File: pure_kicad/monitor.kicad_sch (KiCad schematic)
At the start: 46 parts, among them J3 XT60M, J4 XT60M, J5 Conn_01x04_Pin, J6 Conn_01x04_Pin, Q5 Q_PMOS_SGD, Q6 Q_NMOS_DGS, Q8 Q_NMOS_DGS, U2 BQ40Z80RSMR

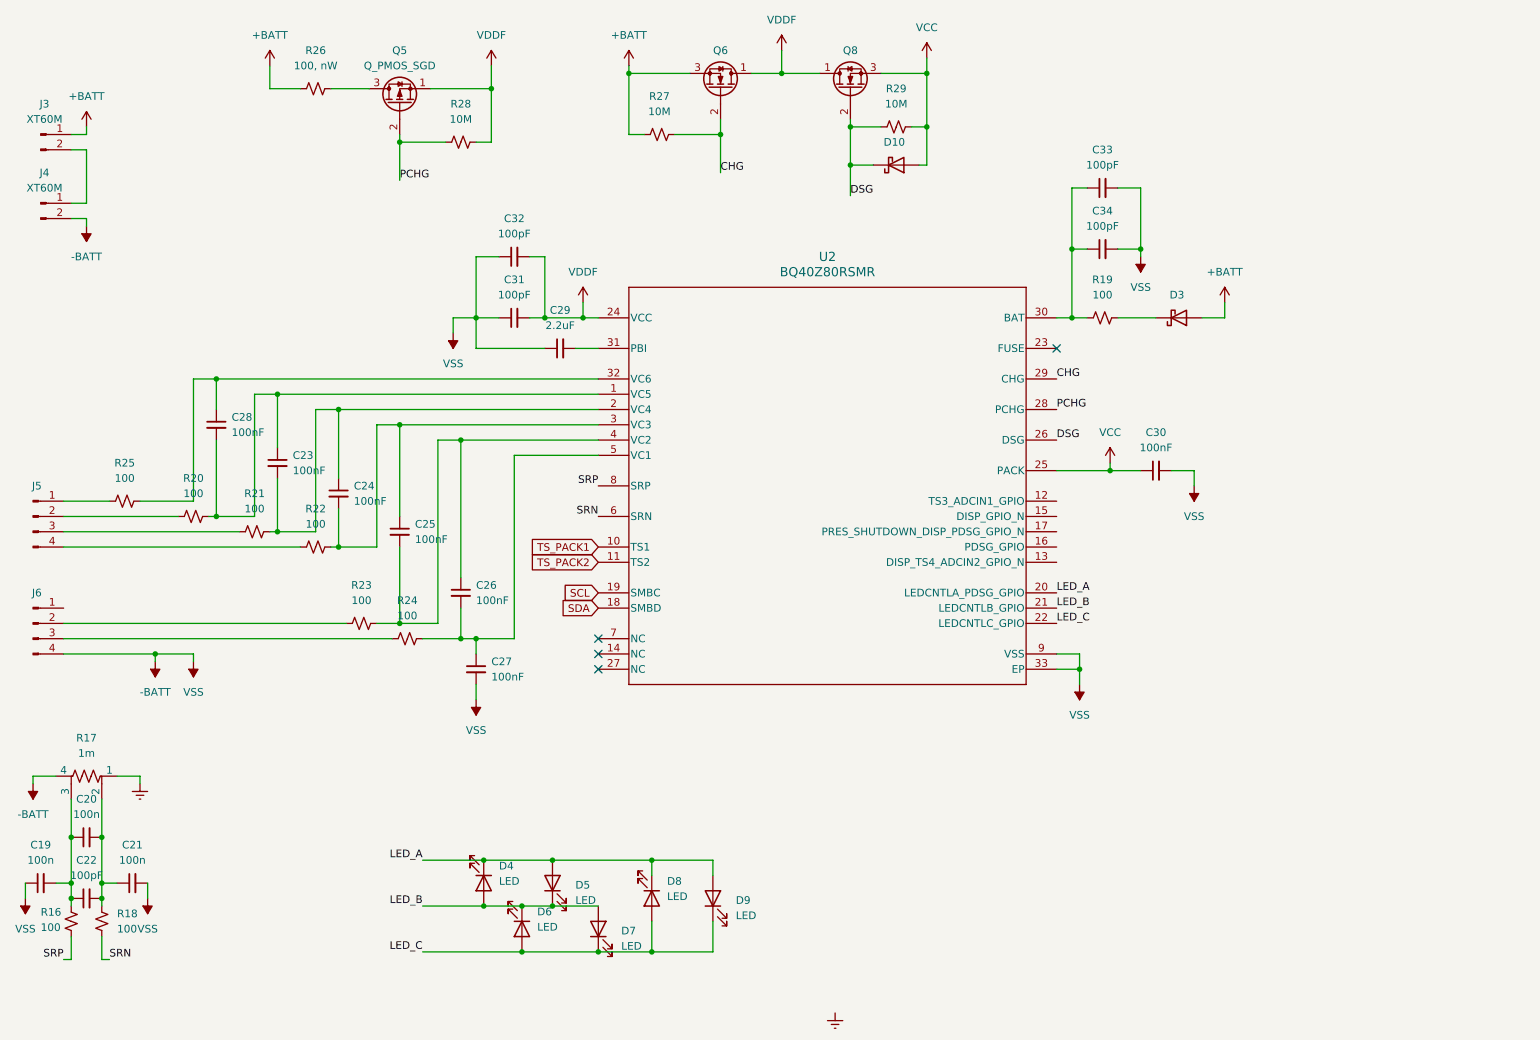
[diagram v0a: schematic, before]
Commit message: Assign parts, start layout
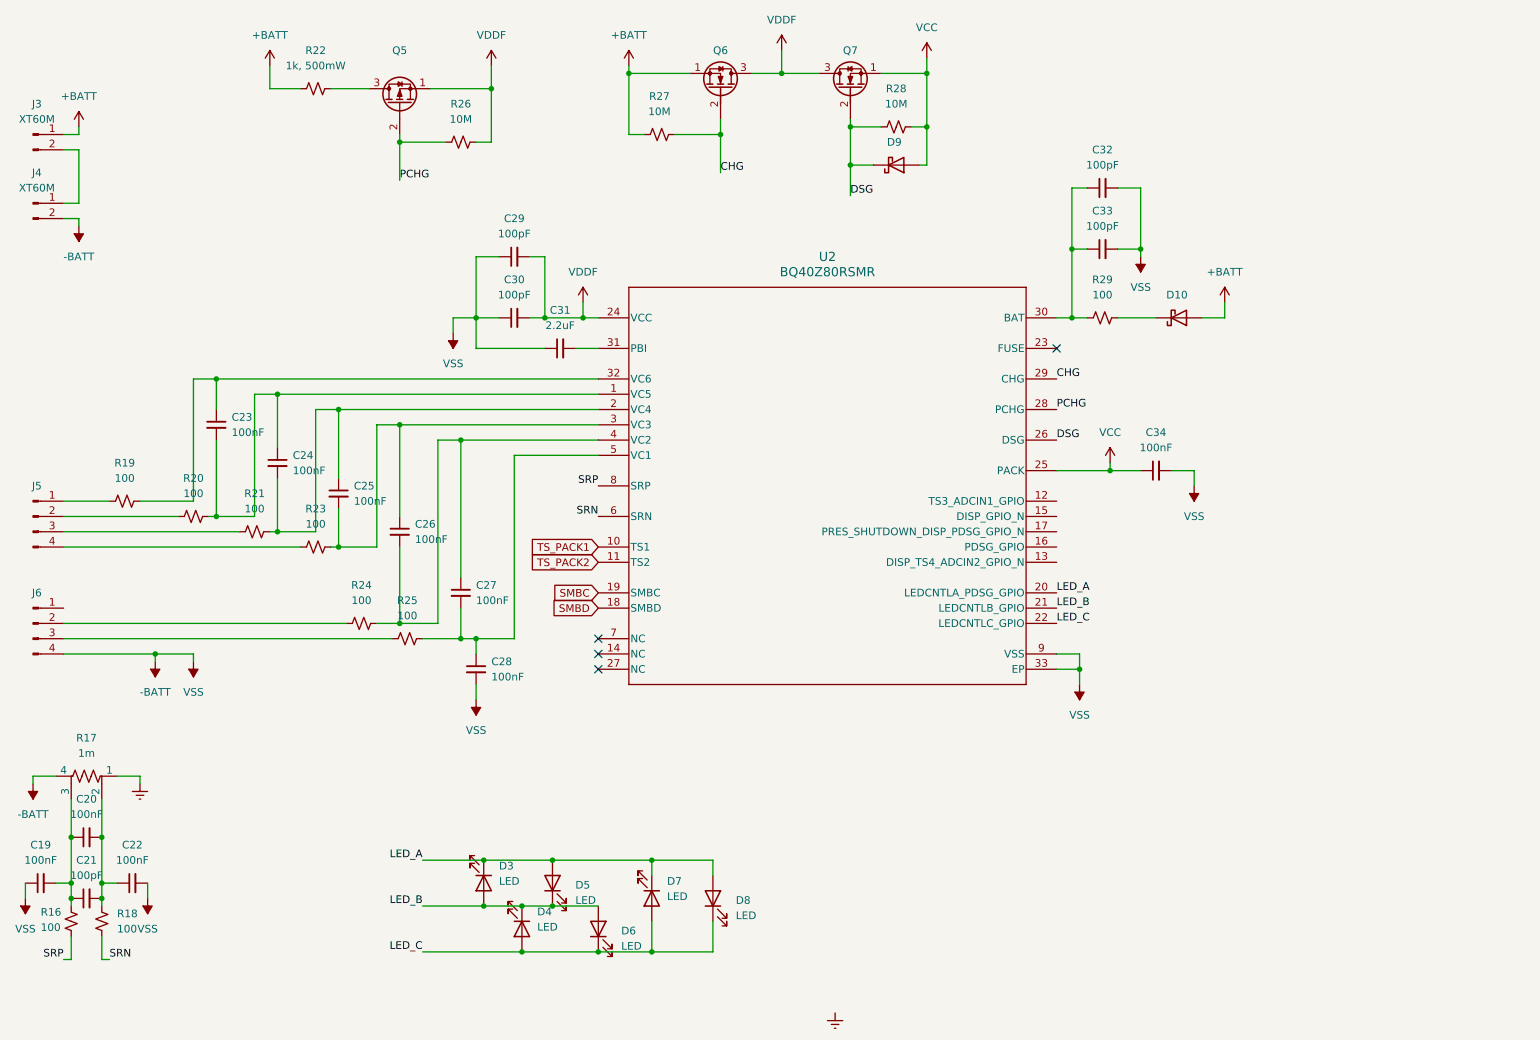
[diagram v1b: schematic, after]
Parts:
- C19, C20: value 100n -> 100nF; footprint Capacitor_SMD:C_0402_1005Metric_Pad0.74x0.62mm_HandSolder -> Capacitor_SMD:C_0603_1608Metric_Pad1.08x0.95mm_HandSolder
- C21: renamed from C22; footprint Capacitor_SMD:C_0402_1005Metric_Pad0.74x0.62mm_HandSolder -> Capacitor_SMD:C_0603_1608Metric_Pad1.08x0.95mm_HandSolder
- C22: renamed from C21; value 100n -> 100nF; footprint Capacitor_SMD:C_0402_1005Metric_Pad0.74x0.62mm_HandSolder -> Capacitor_SMD:C_0603_1608Metric_Pad1.08x0.95mm_HandSolder
- C23: renamed from C28; footprint (none) -> Capacitor_SMD:C_0603_1608Metric_Pad1.08x0.95mm_HandSolder
- C24: renamed from C23; footprint (none) -> Capacitor_SMD:C_0603_1608Metric_Pad1.08x0.95mm_HandSolder
- C25: renamed from C24; footprint (none) -> Capacitor_SMD:C_0603_1608Metric_Pad1.08x0.95mm_HandSolder
- C26: renamed from C25; footprint (none) -> Capacitor_SMD:C_0603_1608Metric_Pad1.08x0.95mm_HandSolder
- C27: renamed from C26; footprint (none) -> Capacitor_SMD:C_0603_1608Metric_Pad1.08x0.95mm_HandSolder
- C28: renamed from C27; footprint (none) -> Capacitor_SMD:C_0603_1608Metric_Pad1.08x0.95mm_HandSolder
- C29: renamed from C32; footprint Capacitor_SMD:C_0402_1005Metric_Pad0.74x0.62mm_HandSolder -> Capacitor_SMD:C_0603_1608Metric_Pad1.08x0.95mm_HandSolder
- C30: renamed from C31; footprint Capacitor_SMD:C_0402_1005Metric_Pad0.74x0.62mm_HandSolder -> Capacitor_SMD:C_0603_1608Metric_Pad1.08x0.95mm_HandSolder
- C31: renamed from C29; footprint Capacitor_SMD:C_0402_1005Metric_Pad0.74x0.62mm_HandSolder -> Capacitor_SMD:C_0603_1608Metric_Pad1.08x0.95mm_HandSolder
- C32: renamed from C33; footprint Capacitor_SMD:C_0402_1005Metric_Pad0.74x0.62mm_HandSolder -> Capacitor_SMD:C_0603_1608Metric_Pad1.08x0.95mm_HandSolder
- C33: renamed from C34; footprint Capacitor_SMD:C_0402_1005Metric_Pad0.74x0.62mm_HandSolder -> Capacitor_SMD:C_0603_1608Metric_Pad1.08x0.95mm_HandSolder
- C34: renamed from C30; footprint (none) -> Capacitor_SMD:C_0603_1608Metric_Pad1.08x0.95mm_HandSolder
- D10: renamed from D3; footprint (none) -> Diode_SMD:D_SMA_Handsoldering
- D9: renamed from D10; footprint (none) -> Diode_SMD:D_SMA_Handsoldering
- Q5: footprint (none) -> cyberec:DFN-8_L3.0-W3.0-P0.65-BL-4
- Q6: footprint (none) -> cyberec:DFN-8_L3.0-W3.0-P0.65-BL-4; symbol Transistor_FET:Q_NMOS_DGS -> Transistor_FET:Q_NMOS_SGD
- Q7: renamed from Q8; footprint (none) -> cyberec:DFN-8_L3.0-W3.0-P0.65-BL-4; symbol Transistor_FET:Q_NMOS_DGS -> Transistor_FET:Q_NMOS_SGD
- R17: footprint (none) -> cyberec:R1206-sense-handsolder
- R18, R20, R21: footprint Resistor_SMD:R_0402_1005Metric_Pad0.72x0.64mm_HandSolder -> Resistor_SMD:R_0603_1608Metric_Pad0.98x0.95mm_HandSolder
- R19: renamed from R25; footprint Resistor_SMD:R_0402_1005Metric_Pad0.72x0.64mm_HandSolder -> Resistor_SMD:R_0603_1608Metric_Pad0.98x0.95mm_HandSolder
- R22: renamed from R26; value 100, nW -> 1k, 500mW; footprint Resistor_SMD:R_0402_1005Metric_Pad0.72x0.64mm_HandSolder -> Resistor_SMD:R_1210_3225Metric_Pad1.30x2.65mm_HandSolder
- R23: renamed from R22; footprint Resistor_SMD:R_0402_1005Metric_Pad0.72x0.64mm_HandSolder -> Resistor_SMD:R_0603_1608Metric_Pad0.98x0.95mm_HandSolder
- R24: renamed from R23; footprint Resistor_SMD:R_0402_1005Metric_Pad0.72x0.64mm_HandSolder -> Resistor_SMD:R_0603_1608Metric_Pad0.98x0.95mm_HandSolder
- R25: renamed from R24; footprint Resistor_SMD:R_0402_1005Metric_Pad0.72x0.64mm_HandSolder -> Resistor_SMD:R_0603_1608Metric_Pad0.98x0.95mm_HandSolder
- R29: renamed from R19; footprint Resistor_SMD:R_0402_1005Metric_Pad0.72x0.64mm_HandSolder -> Resistor_SMD:R_0603_1608Metric_Pad0.98x0.95mm_HandSolder
- renumbered D4 to D3, D6 to D4, D7 to D6, D8 to D7, D9 to D8, R28 to R26, R29 to R28
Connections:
- net +BATT: now also Q6.1 (S); no longer Q6.3 (S)
- net VCC: now also Q7.1 (S); no longer Q7.3 (S)
- net VDDF: now also Q6.3 (D), Q7.3 (D); no longer Q6.1 (D), Q7.1 (D)
- net SCL renamed SMBC
- net SDA renamed SMBD
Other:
- moved on the sheet: J3, J4

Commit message: Layout starting to look alright
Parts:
- R16: footprint Resistor_SMD:R_0402_1005Metric_Pad0.72x0.64mm_HandSolder -> Resistor_SMD:R_0603_1608Metric_Pad0.98x0.95mm_HandSolder
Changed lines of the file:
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@@
 			)
 		)
-		(property "Footprint" "Resistor_SMD:R_0402_1005Metric_Pad0.72x0.64mm_HandSolder"
+		(property "Footprint" "Resistor_SMD:R_0603_1608Metric_Pad0.98x0.95mm_HandSolder"
 			(at 36.83 173.99 0)
 			(effects

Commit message: Import all the footprints, use project local 3d files
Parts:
- C19, C20, C21, C22, C23, C24, C25, C26, C27, C28, C29, C30, C31, C32, C33, C34: footprint Capacitor_SMD:C_0603_1608Metric_Pad1.08x0.95mm_HandSolder -> cyberec:C_0603_1608Metric_Pad1.08x0.95mm_HandSolder
- D10, D9: footprint Diode_SMD:D_SMA_Handsoldering -> cyberec:D_SMA_Handsoldering
- D3, D4, D5, D6, D7, D8: footprint LED_SMD:LED_0603_1608Metric_Pad1.05x0.95mm_HandSolder -> cyberec:LED_0603_1608Metric_Pad1.05x0.95mm_HandSolder
- J3, J4: footprint Connector_AMASS:AMASS_XT60-M_1x02_P7.20mm_Vertical -> cyberec:AMASS_XT60-M_1x02_P7.20mm_Vertical
- J5, J6: footprint Connector_JST:JST_XH_B4B-XH-A_1x04_P2.50mm_Vertical -> cyberec:JST_XH_B4B-XH-A_1x04_P2.50mm_Vertical
- R16, R18, R19, R20, R21, R23, R24, R25, R29: footprint Resistor_SMD:R_0603_1608Metric_Pad0.98x0.95mm_HandSolder -> cyberec:R_0603_1608Metric_Pad0.98x0.95mm_HandSolder
- R22: footprint Resistor_SMD:R_1210_3225Metric_Pad1.30x2.65mm_HandSolder -> cyberec:R_1210_3225Metric_Pad1.30x2.65mm_HandSolder
- R26, R27, R28: footprint Resistor_SMD:R_0402_1005Metric_Pad0.72x0.64mm_HandSolder -> cyberec:R_0402_1005Metric_Pad0.72x0.64mm_HandSolder
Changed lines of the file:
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@@
 			)
 		)
-		(property "Footprint" "LED_SMD:LED_0603_1608Metric_Pad1.05x0.95mm_HandSolder"
+		(property "Footprint" "cyberec:LED_0603_1608Metric_Pad1.05x0.95mm_HandSolder"
 			(at 105.41 167.64 0)
 			(effects
@@
 			)
 		)
-		(property "Footprint" "Resistor_SMD:R_0603_1608Metric_Pad0.98x0.95mm_HandSolder"
+		(property "Footprint" "cyberec:R_0603_1608Metric_Pad0.98x0.95mm_HandSolder"
 			(at 77.47 111.76 0)
 			(effects
@@
 			)
 		)
-		(property "Footprint" "Connector_JST:JST_XH_B4B-XH-A_1x04_P2.50mm_Vertical"
+		(property "Footprint" "cyberec:JST_XH_B4B-XH-A_1x04_P2.50mm_Vertical"
 			(at 30.48 106.68 0)
 			(effects
@@
 			)
 		)
-		(property "Footprint" "Resistor_SMD:R_0603_1608Metric_Pad0.98x0.95mm_HandSolder"
+		(property "Footprint" "cyberec:R_0603_1608Metric_Pad0.98x0.95mm_HandSolder"
 			(at 45.72 104.14 0)
 			(effects
@@
 			)
 		)
-		(property "Footprint" "Capacitor_SMD:C_0603_1608Metric_Pad1.08x0.95mm_HandSolder"
+		(property "Footprint" "cyberec:C_0603_1608Metric_Pad1.08x0.95mm_HandSolder"
 			(at 31.75 167.64 0)
 			(effects
@@
 			)
 		)
-		(property "Footprint" "Capacitor_SMD:C_0603_1608Metric_Pad1.08x0.95mm_HandSolder"
+		(property "Footprint" "cyberec:C_0603_1608Metric_Pad1.08x0.95mm_HandSolder"
 			(at 71.12 97.79 0)
 			(effects
@@
 			)
 		)
-		(property "Footprint" "Capacitor_SMD:C_0603_1608Metric_Pad1.08x0.95mm_HandSolder"
+		(property "Footprint" "cyberec:C_0603_1608Metric_Pad1.08x0.95mm_HandSolder"
 			(at 217.17 99.06 0)
 			(effects
@@
 			)
 		)
-		(property "Footprint" "Resistor_SMD:R_0402_1005Metric_Pad0.72x0.64mm_HandSolder"
+		(property "Footprint" "cyberec:R_0402_1005Metric_Pad0.72x0.64mm_HandSolder"
 			(at 134.62 43.18 0)
 			(effects
@@
 			)
 		)
-		(property "Footprint" "Diode_SMD:D_SMA_Handsoldering"
+		(property "Footprint" "cyberec:D_SMA_Handsoldering"
 			(at 173.99 48.26 0)
 			(effects
@@
 			)
 		)
-		(property "Footprint" "Capacitor_SMD:C_0603_1608Metric_Pad1.08x0.95mm_HandSolder"
+		(property "Footprint" "cyberec:C_0603_1608Metric_Pad1.08x0.95mm_HandSolder"
 			(at 208.28 52.07 0)
 			(effects
@@
 			)
 		)
-		(property "Footprint" "Diode_SMD:D_SMA_Handsoldering"
+		(property "Footprint" "cyberec:D_SMA_Handsoldering"
 			(at 220.98 73.66 0)
 			(effects
@@
 			)
 		)
-		(property "Footprint" "Resistor_SMD:R_1210_3225Metric_Pad1.30x2.65mm_HandSolder"
+		(property "Footprint" "cyberec:R_1210_3225Metric_Pad1.30x2.65mm_HandSolder"
 			(at 77.47 35.56 0)
 			(effects
@@
 			)
 		)
-		(property "Footprint" "Capacitor_SMD:C_0603_1608Metric_Pad1.08x0.95mm_HandSolder"
+		(property "Footprint" "cyberec:C_0603_1608Metric_Pad1.08x0.95mm_HandSolder"
 			(at 110.49 63.5 0)
 			(effects
@@
 			)
 		)
-		(property "Footprint" "Resistor_SMD:R_0603_1608Metric_Pad0.98x0.95mm_HandSolder"
+		(property "Footprint" "cyberec:R_0603_1608Metric_Pad0.98x0.95mm_HandSolder"
 			(at 85.09 124.46 0)
 			(effects
@@
 			)
 		)
-		(property "Footprint" "Resistor_SMD:R_0603_1608Metric_Pad0.98x0.95mm_HandSolder"
+		(property "Footprint" "cyberec:R_0603_1608Metric_Pad0.98x0.95mm_HandSolder"
 			(at 92.71 127 0)
 			(effects
@@
 			)
 		)
-		(property "Footprint" "Resistor_SMD:R_0603_1608Metric_Pad0.98x0.95mm_HandSolder"
+		(property "Footprint" "cyberec:R_0603_1608Metric_Pad0.98x0.95mm_HandSolder"
 			(at 36.83 173.99 0)
 			(effects
@@
 			)
 		)
-		(property "Footprint" "Connector_AMASS:AMASS_XT60-M_1x02_P7.20mm_Vertical"
+		(property "Footprint" "cyberec:AMASS_XT60-M_1x02_P7.20mm_Vertical"
 			(at 30.48 43.18 0)
 			(effects
@@
 			)
 		)
-		(property "Footprint" "LED_SMD:LED_0603_1608Metric_Pad1.05x0.95mm_HandSolder"
+		(property "Footprint" "cyberec:LED_0603_1608Metric_Pad1.05x0.95mm_HandSolder"
 			(at 133.35 170.18 0)
 			(effects
@@
 			)
 		)
-		(property "Footprint" "LED_SMD:LED_0603_1608Metric_Pad1.05x0.95mm_HandSolder"
+		(property "Footprint" "cyberec:LED_0603_1608Metric_Pad1.05x0.95mm_HandSolder"
 			(at 124.46 175.26 0)
 			(effects
@@
 			)
 		)
-		(property "Footprint" "Resistor_SMD:R_0603_1608Metric_Pad0.98x0.95mm_HandSolder"
+		(property "Footprint" "cyberec:R_0603_1608Metric_Pad0.98x0.95mm_HandSolder"
 			(at 57.15 106.68 0)
 			(effects
@@
 			)
 		)
-		(property "Footprint" "Capacitor_SMD:C_0603_1608Metric_Pad1.08x0.95mm_HandSolder"
+		(property "Footprint" "cyberec:C_0603_1608Metric_Pad1.08x0.95mm_HandSolder"
 			(at 91.44 109.22 0)
 			(effects
@@
 			)
 		)
-		(property "Footprint" "Capacitor_SMD:C_0603_1608Metric_Pad1.08x0.95mm_HandSolder"
+		(property "Footprint" "cyberec:C_0603_1608Metric_Pad1.08x0.95mm_HandSolder"
 			(at 60.96 91.44 0)
 			(effects
@@
 			)
 		)
-		(property "Footprint" "Capacitor_SMD:C_0603_1608Metric_Pad1.08x0.95mm_HandSolder"
+		(property "Footprint" "cyberec:C_0603_1608Metric_Pad1.08x0.95mm_HandSolder"
 			(at 104.14 132.08 0)
 			(effects
@@
 			)
 		)
-		(property "Footprint" "Capacitor_SMD:C_0603_1608Metric_Pad1.08x0.95mm_HandSolder"
+		(property "Footprint" "cyberec:C_0603_1608Metric_Pad1.08x0.95mm_HandSolder"
 			(at 81.28 102.87 0)
 			(effects
@@
 			)
 		)
-		(property "Footprint" "Capacitor_SMD:C_0603_1608Metric_Pad1.08x0.95mm_HandSolder"
+		(property "Footprint" "cyberec:C_0603_1608Metric_Pad1.08x0.95mm_HandSolder"
 			(at 118.11 78.74 0)
 			(effects
@@
 			)
 		)
-		(property "Footprint" "LED_SMD:LED_0603_1608Metric_Pad1.05x0.95mm_HandSolder"
+		(property "Footprint" "cyberec:LED_0603_1608Metric_Pad1.05x0.95mm_HandSolder"
 			(at 116.84 167.64 0)
 			(effects
@@
 			)
 		)
-		(property "Footprint" "Resistor_SMD:R_0603_1608Metric_Pad0.98x0.95mm_HandSolder"
+		(property "Footprint" "cyberec:R_0603_1608Metric_Pad0.98x0.95mm_HandSolder"
 			(at 208.28 73.66 0)
 			(effects
@@
 			)
 		)
-		(property "Footprint" "Resistor_SMD:R_0603_1608Metric_Pad0.98x0.95mm_HandSolder"
+		(property "Footprint" "cyberec:R_0603_1608Metric_Pad0.98x0.95mm_HandSolder"
 			(at 41.91 173.99 0)
 			(effects
@@
 			)
 		)
-		(property "Footprint" "Capacitor_SMD:C_0603_1608Metric_Pad1.08x0.95mm_HandSolder"
+		(property "Footprint" "cyberec:C_0603_1608Metric_Pad1.08x0.95mm_HandSolder"
 			(at 110.49 73.66 0)
 			(effects
@@
 			)
 		)
-		(property "Footprint" "Capacitor_SMD:C_0603_1608Metric_Pad1.08x0.95mm_HandSolder"
+		(property "Footprint" "cyberec:C_0603_1608Metric_Pad1.08x0.95mm_HandSolder"
 			(at 208.28 62.23 0)
 			(effects
@@
 			)
 		)
-		(property "Footprint" "Capacitor_SMD:C_0603_1608Metric_Pad1.08x0.95mm_HandSolder"
+		(property "Footprint" "cyberec:C_0603_1608Metric_Pad1.08x0.95mm_HandSolder"
 			(at 101.6 119.38 0)
 			(effects
@@
 			)
 		)
-		(property "Footprint" "Resistor_SMD:R_0603_1608Metric_Pad0.98x0.95mm_HandSolder"
+		(property "Footprint" "cyberec:R_0603_1608Metric_Pad0.98x0.95mm_HandSolder"
 			(at 67.31 109.22 0)
 			(effects
@@
 			)
 		)
-		(property "Footprint" "Resistor_SMD:R_0402_1005Metric_Pad0.72x0.64mm_HandSolder"
+		(property "Footprint" "cyberec:R_0402_1005Metric_Pad0.72x0.64mm_HandSolder"
 			(at 101.6 44.45 0)
 			(effects
@@
 			)
 		)
-		(property "Footprint" "Connector_AMASS:AMASS_XT60-M_1x02_P7.20mm_Vertical"
+		(property "Footprint" "cyberec:AMASS_XT60-M_1x02_P7.20mm_Vertical"
 			(at 30.48 54.61 0)
 			(effects
@@
 			)
 		)
-		(property "Footprint" "LED_SMD:LED_0603_1608Metric_Pad1.05x0.95mm_HandSolder"
+		(property "Footprint" "cyberec:LED_0603_1608Metric_Pad1.05x0.95mm_HandSolder"
 			(at 111.76 175.26 0)
 			(effects
@@
 			)
 		)
-		(property "Footprint" "LED_SMD:LED_0603_1608Metric_Pad1.05x0.95mm_HandSolder"
+		(property "Footprint" "cyberec:LED_0603_1608Metric_Pad1.05x0.95mm_HandSolder"
 			(at 143.51 170.18 0)
 			(effects
@@
 			)
 		)
-		(property "Footprint" "Capacitor_SMD:C_0603_1608Metric_Pad1.08x0.95mm_HandSolder"
+		(property "Footprint" "cyberec:C_0603_1608Metric_Pad1.08x0.95mm_HandSolder"
 			(at 39.37 170.18 0)
 			(effects
@@
 			)
 		)
-		(property "Footprint" "Resistor_SMD:R_0402_1005Metric_Pad0.72x0.64mm_HandSolder"
+		(property "Footprint" "cyberec:R_0402_1005Metric_Pad0.72x0.64mm_HandSolder"
 			(at 173.99 41.91 0)
 			(effects
@@
 			)
 		)
-		(property "Footprint" "Capacitor_SMD:C_0603_1608Metric_Pad1.08x0.95mm_HandSolder"
+		(property "Footprint" "cyberec:C_0603_1608Metric_Pad1.08x0.95mm_HandSolder"
 			(at 39.37 160.02 0)
 			(effects
@@
 			)
 		)
-		(property "Footprint" "Connector_JST:JST_XH_B4B-XH-A_1x04_P2.50mm_Vertical"
+		(property "Footprint" "cyberec:JST_XH_B4B-XH-A_1x04_P2.50mm_Vertical"
 			(at 30.48 124.46 0)
 			(effects
@@
 			)
 		)
-		(property "Footprint" "Capacitor_SMD:C_0603_1608Metric_Pad1.08x0.95mm_HandSolder"
+		(property "Footprint" "cyberec:C_0603_1608Metric_Pad1.08x0.95mm_HandSolder"
 			(at 46.99 167.64 0)
 			(effects
